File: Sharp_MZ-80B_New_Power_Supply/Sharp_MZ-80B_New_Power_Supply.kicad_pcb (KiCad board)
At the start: 2 copper layers, 139 x 125 mm, 16 parts, among them J1 To Motherboard, J2 DC In, J3 To Tape Deck, J4 To Monitor, U1 PSU5, U2 R-78CK5.0-0.5

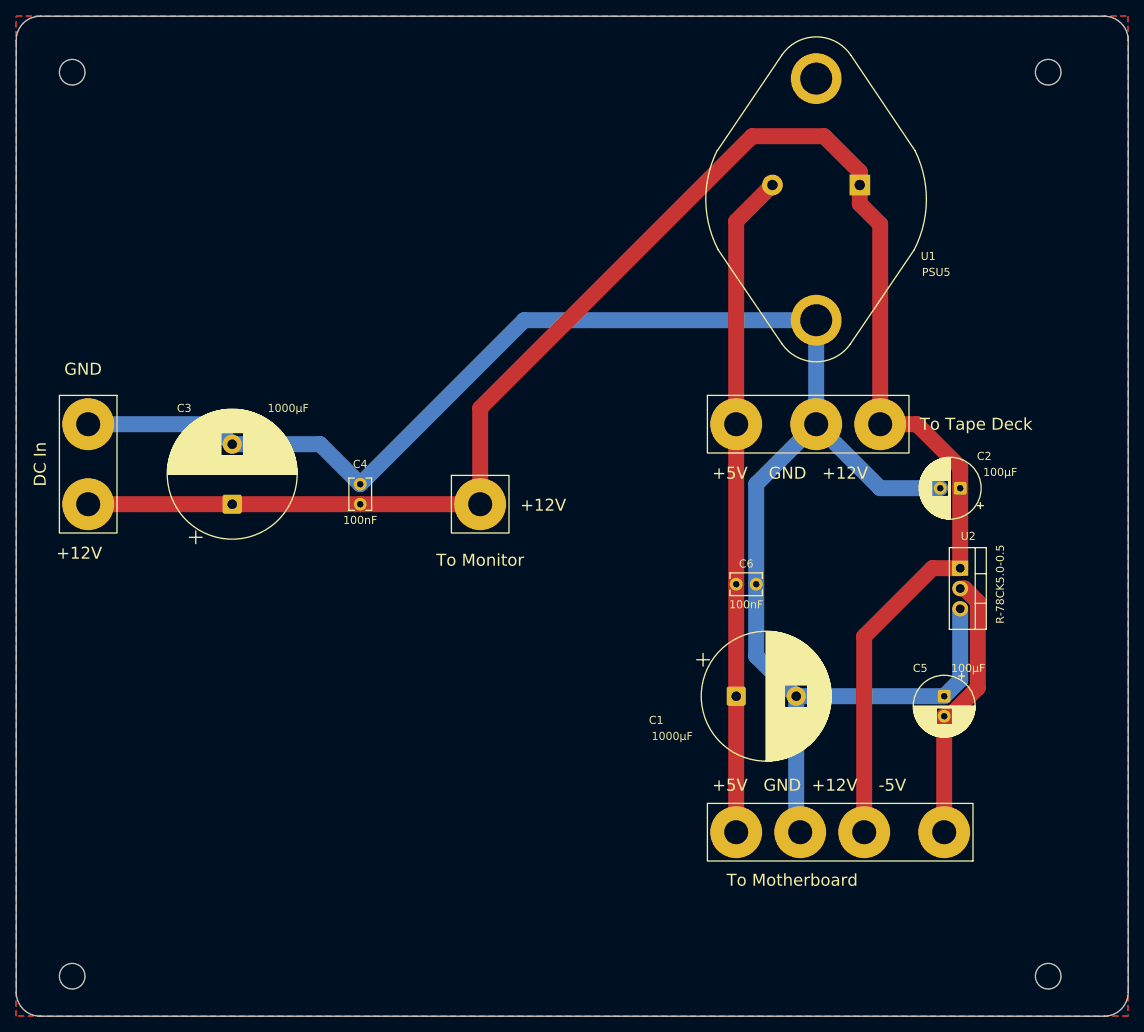
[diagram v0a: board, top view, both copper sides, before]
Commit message: Update design to use +15VDC in
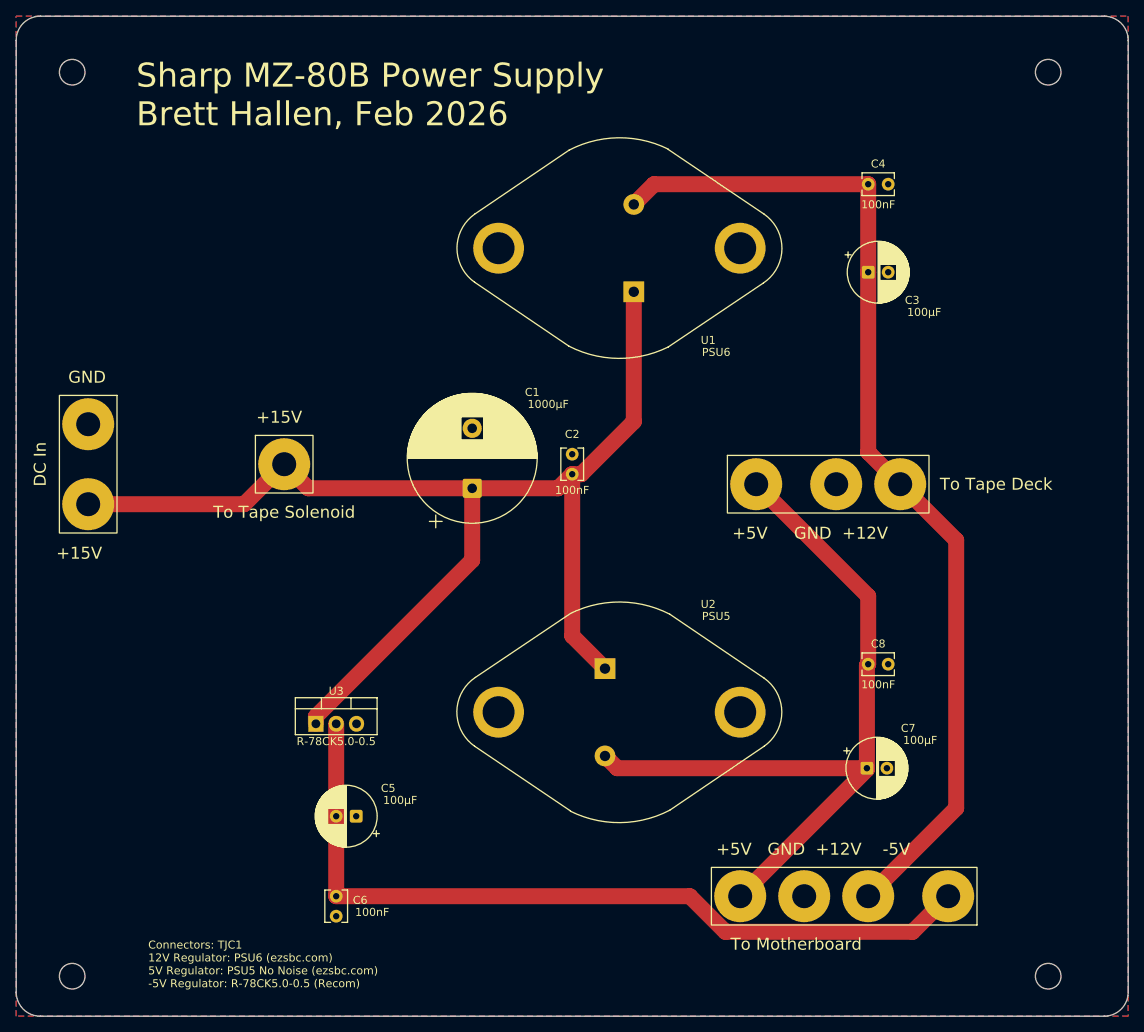
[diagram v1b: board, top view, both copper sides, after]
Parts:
- removed the C1 at (173.5, 118.0)
- removed the C2 at (201.5, 92.0)
- removed the U2 at (201.5, 102.0)
- added C3: 100µF, Capacitor_THT:CP_Radial_D7.5mm_P2.50mm, F.Cu at (190.0, 65.0)
- added C4: 100nF, Capacitor_THT:C_Disc_D3.8mm_W2.6mm_P2.50mm, F.Cu at (190.0, 54.0)
- added C7: 100µF, Capacitor_THT:CP_Radial_D7.5mm_P2.50mm, F.Cu at (189.8, 127.0)
- added C8: 100nF, Capacitor_THT:C_Disc_D3.8mm_W2.6mm_P2.50mm, F.Cu at (190.0, 114.0)
- added U1: PSU6, Package_TO_SOT_THT:TO-3, F.Cu at (160.7, 67.5)
- added U3: R-78CK5.0-0.5, Package_TO_SOT_THT:TO-220-3_Vertical, F.Cu at (121.0, 121.5)
- J1: renamed from J4; value To Monitor -> To Tape Solenoid
- moved C5 75.0 mm to (126.0, 133.0), turned to 180 degrees
- moved U2 68.3 mm to (157.1, 114.5), turned to 0 degrees
- moved C6 63.4 mm to (123.5, 143.0), turned to -90 degrees
- moved C1 30.1 mm to (140.5, 92.0)
- moved C2 26.8 mm to (153.0, 90.2)
- moved J1 25.0 mm to (117.0, 89.0)
- moved J3 8.02 mm to (200.0, 143.0)
- moved J4 7.91 mm to (176.0, 91.5)
- renumbered C3 to C1, C4 to C2, J1 to J3, J3 to J4, U1 to U2
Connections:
- C1 pad 1: /+12V -> /+15V
- C2 pad 1: /+12V -> /+15V
- C6 pad 1: /+5V -> /-5V
- J1 pad 1: /+12V -> /+15V
- J2 pad 2: /+12V -> /+15V
- U2 pad 1: /+12V -> /+15V
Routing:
- net /GND: track 221.0 -> 0.00 mm
- net /+15V: track 0.00 -> 154.7 mm
- net /+12V: track 221.8 -> 128.5 mm
- net /-5V: track 33.8 -> 101.7 mm
- net /+5V: track 82.8 -> 97.3 mm
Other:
- board text added: "+15V"
- board text added: "Connectors: TJC1 12V Regulator: PSU6 (ezsbc.com) 5V Regulator: PSU5 No Noise (ezsbc.com) -5V Regulator: R-78CK5.0-0.5 (Recom)"
- board text added: "Sharp MZ-80B Power Supply Brett Hallen, Feb 2026"
- board text removed: "+12V"
